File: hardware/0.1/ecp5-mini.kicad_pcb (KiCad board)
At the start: 4 copper layers, 52 x 27 mm, 7 parts, among them J1 Conn_01x40_Male, J2 Conn_01x40_Male

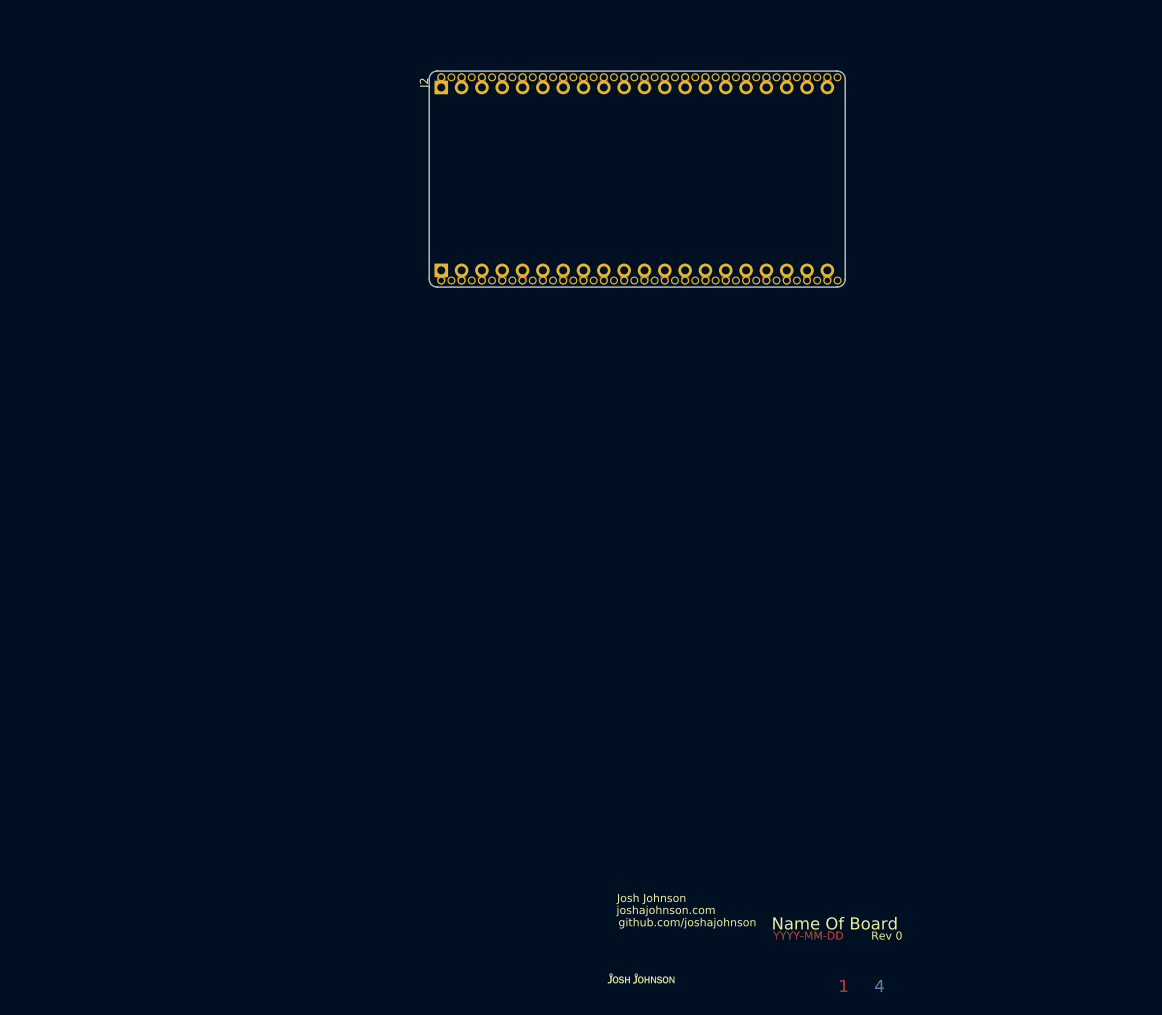
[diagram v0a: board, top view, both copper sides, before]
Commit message: looks like it will fit
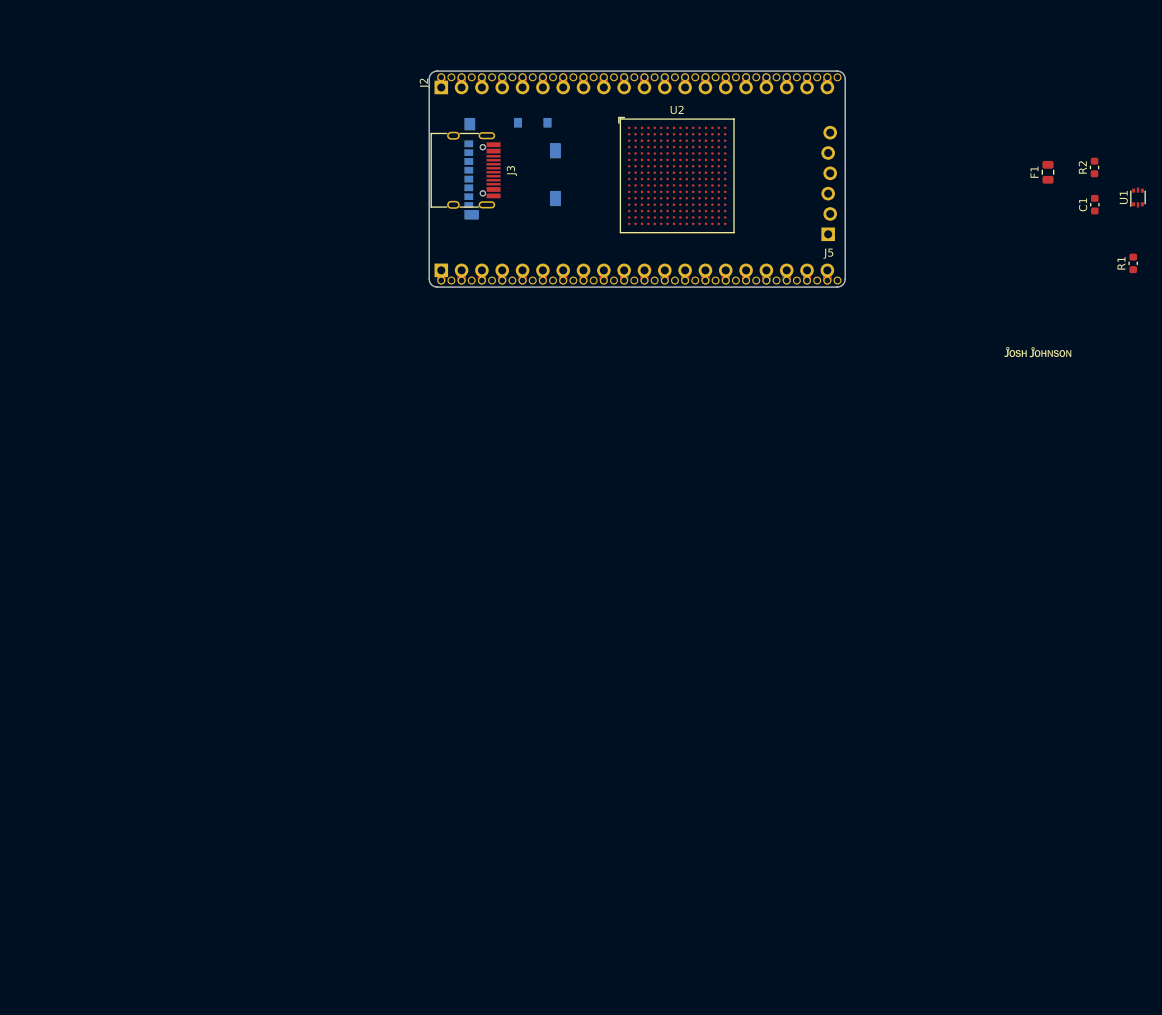
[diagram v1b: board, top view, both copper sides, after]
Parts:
- removed LOGO1: Josh-Details, josh-logos:josh-details
- removed LOGO3: Board-Title, josh-logos:board-title
- removed LOGO5: 4-Layer-Check, josh-logos:4-layer-check
- added C1: 4u7, Capacitor_SMD:C_0603_1608Metric, F.Cu at (199.8, 97.2)
- added F1: 1A, josh-passives-smt:Fuse_0805_2012Metric, F.Cu at (193.9, 93.2)
- added J3: USB_C_Receptacle_USB2.0, josh-connectors:USB_C_U262-161N-4BVC11, F.Cu at (121.5, 92.9)
- added J4: Micro_SD_Card, Connector_Card:microSD_HC_Molex_104031-0811, B.Cu at (127.0, 92.7)
- added J5: JTAG, josh-connectors:STM_6_PIN_THT_Staggered, F.Cu at (166.6, 100.9)
- added R1: 5K1, Resistor_SMD:R_0603_1608Metric, F.Cu at (204.6, 104.5)
- added R2: 5K1, Resistor_SMD:R_0603_1608Metric, F.Cu at (199.8, 92.5)
- added U1: USBLC6-2SC6, Package_TO_SOT_SMD:SOT-666, F.Cu at (205.2, 96.3)
- added U2: ECP5U_12_CABGA256, Package_BGA:BGA-256_14.0x14.0mm_Layout16x16_P0.8mm_Ball0.45mm_Pad0.32mm_NSMD, F.Cu at (147.6, 93.6)
- J1, J2: value Conn_01x40_Male -> S7 Mini
- moved LOGO2 92.7 mm to (206.8, 115.6)
- moved LOGO4 92.7 mm to (192.7, 115.6)

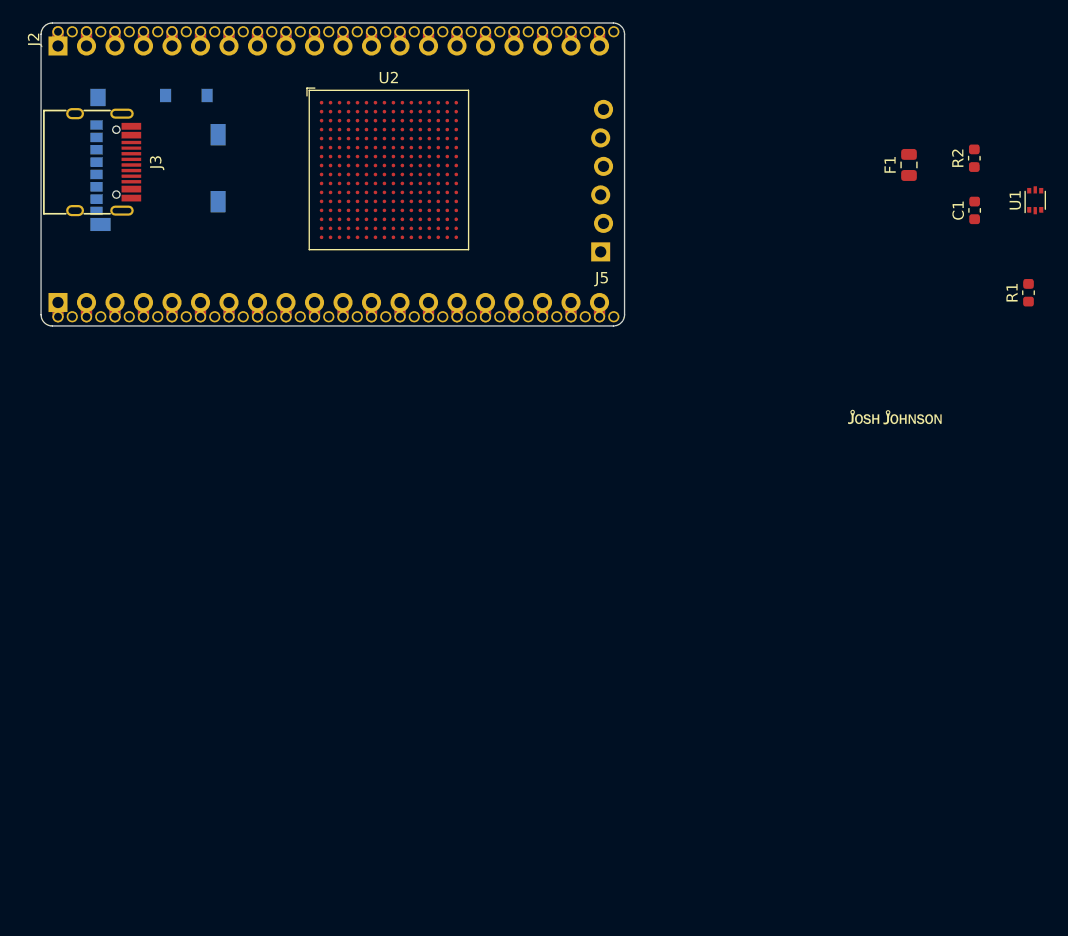
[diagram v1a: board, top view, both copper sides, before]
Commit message: update gitignore
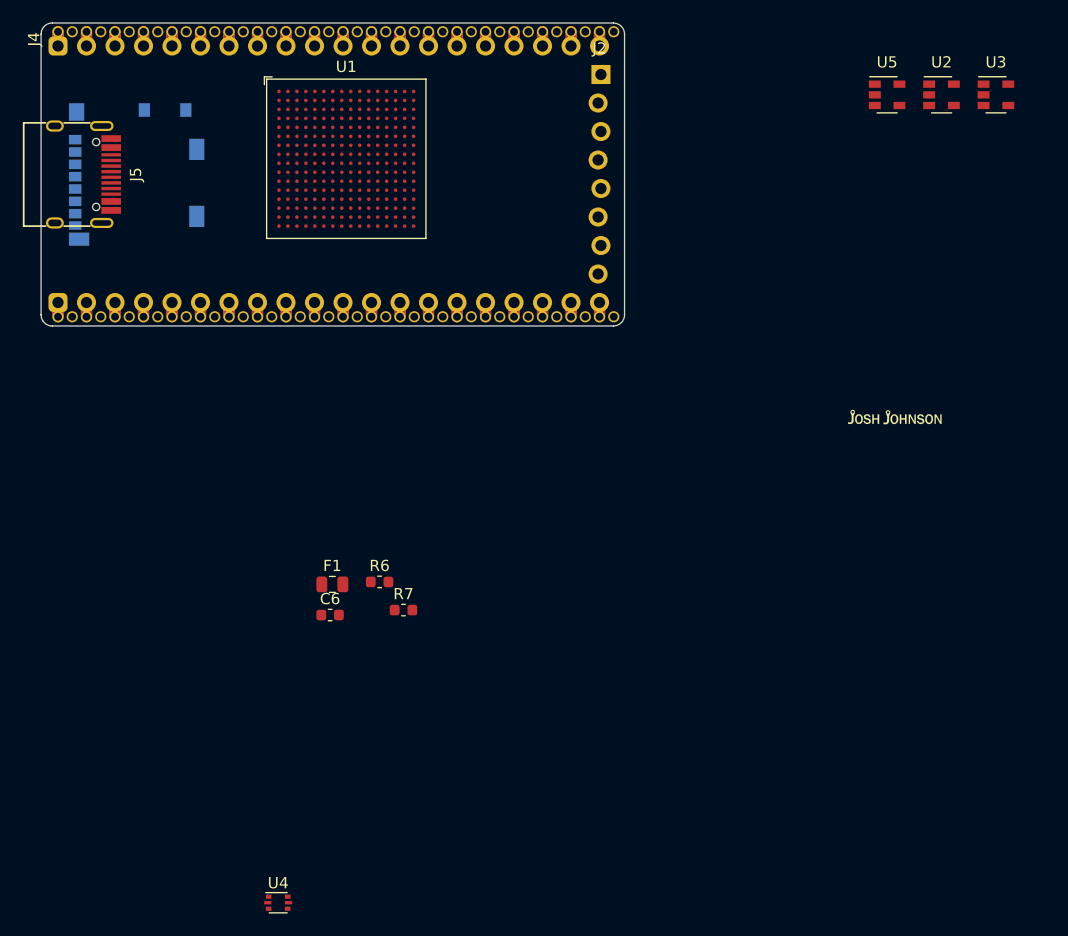
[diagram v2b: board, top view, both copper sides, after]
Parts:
- removed C1: 4u7, Capacitor_SMD:C_0603_1608Metric
- removed R1, R2: 5K1, Resistor_SMD:R_0603_1608Metric
- added C6: 4u7, Capacitor_SMD:C_0603_1608Metric, F.Cu at (142.4, 133.3)
- added R6: 5K1, Resistor_SMD:R_0603_1608Metric, F.Cu at (146.8, 130.3)
- added R7: 5K1, Resistor_SMD:R_0603_1608Metric, F.Cu at (148.9, 132.8)
- added U3: TLV62568DBV, Package_TO_SOT_SMD:SOT-23-5, F.Cu at (201.7, 86.9)
- added U4: USBLC6-2SC6, Package_TO_SOT_SMD:SOT-666, F.Cu at (137.7, 158.9)
- added U5: TLV62568DBV, Package_TO_SOT_SMD:SOT-23-5, F.Cu at (192.0, 86.9)
- J1: value S7 Mini -> Micro_SD_Card; footprint josh-connectors:ECP5-Mini-Edge-20x2.54-40x1.27 -> Connector_Card:microSD_HC_Molex_104031-0811
- J2: value S7 Mini -> JTAG; footprint josh-connectors:ECP5-Mini-Edge-20x2.54-40x1.27 -> josh-connectors:8_PIN_THT_Staggered
- J3: value USB_C_Receptacle_USB2.0 -> S7 Mini; footprint josh-connectors:USB_C_U262-161N-4BVC11 -> josh-connectors:ECP5-Mini-Edge-20x2.54-40x1.27; moved to B.Cu
- J4: value Micro_SD_Card -> S7 Mini; footprint Connector_Card:microSD_HC_Molex_104031-0811 -> josh-connectors:ECP5-Mini-Edge-20x2.54-40x1.27; moved to F.Cu
- J5: value JTAG -> USB_C_Receptacle_USB2.0; footprint josh-connectors:STM_6_PIN_THT_Staggered -> josh-connectors:USB_C_U262-161N-4BVC11
- U1: value USBLC6-2SC6 -> ECP5U_12_CABGA256; footprint Package_TO_SOT_SMD:SOT-666 -> Package_BGA:BGA-256_14.0x14.0mm_Layout16x16_P0.8mm_Ball0.45mm_Pad0.32mm_NSMD
- U2: value ECP5U_12_CABGA256 -> TLV73325PDBV; footprint Package_BGA:BGA-256_14.0x14.0mm_Layout16x16_P0.8mm_Ball0.45mm_Pad0.32mm_NSMD -> Package_TO_SOT_SMD:SOT-23-5
- moved F1 63.5 mm to (142.6, 130.5), turned to 0 degrees
- moved U1 61.5 mm to (143.8, 92.6), turned to 0 degrees
- moved U2 49.7 mm to (196.8, 86.9)
- moved J2 48.3 mm to (166.4, 85.1), turned to 0 degrees
- moved J5 47.4 mm to (119.7, 94.0), turned to -90 degrees
- moved J4 13.5 mm to (118.1, 82.5), turned to 90 degrees
- moved J1 13.4 mm to (125.1, 94.0)
- moved J3 13.0 mm to (118.1, 105.4)
- renumbered LOGO4 to LOGO1
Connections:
- net Net-(J2-Pad5) renamed /FPGA Config/TCK
- net Net-(J2-Pad6) renamed /FPGA Config/TDO
- net Net-(J2-Pad7) renamed /FPGA Config/TDI
- net Net-(J2-Pad8) renamed /FPGA Config/TMS
- F1 pad 1: Net-(C1-Pad1) -> Net-(C6-Pad1)
- F1 pad 2: VBUS -> +5V
- J2 pad 1: Net-(J2-Pad1) -> GND
- J2 pad 2: Net-(J2-Pad2) -> +5V
- J2 pad 3: Net-(J2-Pad3) -> +3V3
- J2 pad 4: Net-(J2-Pad4) -> GND

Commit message: power + leds + hyperram
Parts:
- added C1: 4u7, Capacitor_SMD:C_0603_1608Metric, F.Cu at (154.4, 129.4)
- added C10: 6p8, Capacitor_SMD:C_0603_1608Metric, F.Cu at (162.4, 135.1)
- added C11: 10u, Capacitor_SMD:C_0603_1608Metric, F.Cu at (181.8, 148.6)
- added C12: 100n, Capacitor_SMD:C_0402_1005Metric, F.Cu at (182.0, 152.0)
- added C13: 100n, Capacitor_SMD:C_0402_1005Metric, F.Cu at (180.0, 132.6)
- added C14: 470n, Capacitor_SMD:C_0402_1005Metric, F.Cu at (178.1, 138.4)
- added C15: 100n, Capacitor_SMD:C_0402_1005Metric, F.Cu at (176.1, 133.1)
- added C16: 100n, Capacitor_SMD:C_0402_1005Metric, F.Cu at (182.0, 138.4)
- added C17: 100n, Capacitor_SMD:C_0402_1005Metric, F.Cu at (180.0, 135.5)
- added C18: 100n, Capacitor_SMD:C_0402_1005Metric, F.Cu at (182.0, 141.3)
- added C2: 4u7, Capacitor_SMD:C_0603_1608Metric, F.Cu at (156.9, 129.4)
- added C3: 1u, Capacitor_SMD:C_0603_1608Metric, F.Cu at (164.9, 135.1)
- added C4: 1u, Capacitor_SMD:C_0603_1608Metric, F.Cu at (154.8, 125.4)
- added C5: 10u, Capacitor_SMD:C_0603_1608Metric, F.Cu at (159.8, 130.4)
- added C7: 22u, Capacitor_SMD:C_0603_1608Metric, F.Cu at (164.9, 139.1)
- added C8: 22u, Capacitor_SMD:C_0603_1608Metric, F.Cu at (162.4, 131.1)
- added C9: 6p8, Capacitor_SMD:C_0603_1608Metric, F.Cu at (159.8, 134.5)
- added D1: PINK, LED_SMD:LED_0603_1608Metric, F.Cu at (164.9, 131.1)
- added D2: LED, LED_SMD:LED_0603_1608Metric, F.Cu at (170.7, 121.0)
- added L1: 2u2, Inductor_SMD:L_0805_2012Metric, F.Cu at (159.7, 126.2)
- added L2: 2u2, Inductor_SMD:L_0805_2012Metric, F.Cu at (154.6, 121.2)
- added Q1: BSS138, Package_TO_SOT_SMD:SOT-23, F.Cu at (180.8, 128.9)
- added R1: 210k, Resistor_SMD:R_0402_1005Metric, F.Cu at (157.6, 132.9)
- added R10: 22R, Resistor_SMD:R_0402_1005Metric, F.Cu at (178.1, 132.6)
- added R11: 1K5, Resistor_SMD:R_0402_1005Metric, F.Cu at (182.0, 132.6)
- added R12: 5K1, Resistor_SMD:R_0402_1005Metric, F.Cu at (175.5, 130.2)
- added R13: 1k, Resistor_SMD:R_0402_1005Metric, F.Cu at (182.0, 135.5)
- added R14: 1k, Resistor_SMD:R_0402_1005Metric, F.Cu at (178.1, 135.5)
- added R15: 1k, Resistor_SMD:R_0402_1005Metric, F.Cu at (173.5, 130.3)
- added R16: 1k, Resistor_SMD:R_0402_1005Metric, F.Cu at (180.0, 138.4)
- added R17: 1k, Resistor_SMD:R_0402_1005Metric, F.Cu at (172.5, 127.4)
- added R18: 1k, Resistor_SMD:R_0402_1005Metric, F.Cu at (171.5, 130.3)
- added R19: 5K1, Resistor_SMD:R_0402_1005Metric, F.Cu at (177.5, 128.1)
- added R2: 47k, Resistor_SMD:R_0402_1005Metric, F.Cu at (162.7, 138.6)
- added R20: 51R, Resistor_SMD:R_0402_1005Metric, F.Cu at (171.0, 124.5)
- added R21: 1K5, Resistor_SMD:R_0402_1005Metric, F.Cu at (170.5, 127.4)
- added R3: 84k5, Resistor_SMD:R_0402_1005Metric, F.Cu at (160.1, 137.9)
- added R4: 100k, Resistor_SMD:R_0402_1005Metric, F.Cu at (155.6, 132.9)
- added R5: 5K1, Resistor_SMD:R_0402_1005Metric, F.Cu at (157.2, 125.5)
- added R8: 10K, Resistor_SMD:R_0402_1005Metric, F.Cu at (176.1, 136.1)
- added R9: 22R, Resistor_SMD:R_0402_1005Metric, F.Cu at (174.1, 133.2)
- added RN1: 10k, Resistor_SMD:R_Array_Convex_4x0402, F.Cu at (175.0, 127.3)
- added SW1: SW_Push, josh-buttons-switches:SW_Push_PTS815, F.Cu at (174.2, 122.4)
- added TP1: 2v5, TestPoint:TestPoint_Pad_D1.5mm, F.Cu at (163.7, 126.6)
- added TP2: 3V3, TestPoint:TestPoint_Pad_D1.5mm, F.Cu at (158.6, 121.5)
- added TP3: 1v1, TestPoint:TestPoint_Pad_D1.5mm, F.Cu at (163.7, 121.5)
- added U6: W25Q128JVSIQ, Package_SON:WSON-8-1EP_6x5mm_P1.27mm_EP3.4x4.3mm, F.Cu at (103.7, 96.8)
- added U7: S27KL0641, josh-bga:BGA-24_5x5_6.0x8.0mm, F.Cu at (103.8, 89.5)
- J2: footprint josh-connectors:8_PIN_THT_Staggered -> josh-connectors:STM_6_PIN_THT_Staggered
- R6, R7: footprint Resistor_SMD:R_0603_1608Metric -> Resistor_SMD:R_0402_1005Metric
- moved J2 69.9 mm to (98.4, 101.3), turned to 180 degrees
- moved U1 25.9 mm to (118.0, 94.8), turned to 180 degrees
- moved J5 25.4 mm to (145.1, 95.0), turned to 90 degrees
- moved J3 20.4 mm to (97.7, 106.4)
- moved J4 20.4 mm to (97.7, 83.5)
- moved J1 14.6 mm to (139.7, 95.0), turned to 90 degrees
- moved U5 3.20 mm to (188.9, 86.1), turned to 180 degrees
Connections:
- net Net-(J1-Pad1) renamed /Hyperram / Micro SD/SD.DAT2
- net Net-(J1-Pad10) renamed /Hyperram / Micro SD/SD.DETA
- net Net-(J1-Pad2) renamed /Hyperram / Micro SD/SD.DAT3
- net Net-(J1-Pad3) renamed /Hyperram / Micro SD/SD.CMD
- net Net-(J1-Pad7) renamed /Hyperram / Micro SD/SD.DAT0
- net Net-(J1-Pad8) renamed /Hyperram / Micro SD/SD.DAT1
- net Net-(J1-Pad9) renamed /Hyperram / Micro SD/SD.DETB
- J1 pad 11: Net-(J1-Pad11) -> GND
- J1 pad 4: Net-(J1-Pad4) -> +3V3
- J1 pad 5: Net-(J1-Pad5) -> +3V3
- J1 pad 6: Net-(J1-Pad6) -> GND
- J2 pad 1: GND -> +3V3
- J2 pad 2: +5V -> GND
- J2 pad 3: +3V3 -> /FPGA Config/TCK
- J2 pad 4: GND -> /FPGA Config/TDO
- J2 pad 5: /FPGA Config/TCK -> /FPGA Config/TDI
- J2 pad 6: /FPGA Config/TDO -> /FPGA Config/TMS
- U1 pad L6: Net-(U1-PadL6) -> +3V3
- U1 pad M10: Net-(U1-PadM10) -> /FPGA Config/TDO
- U1 pad M7: Net-(U1-PadM7) -> /FPGA Config/CFG.IO2
- U1 pad N10: Net-(U1-PadN10) -> /FPGA Config/CFG_0
- U1 pad N7: Net-(U1-PadN7) -> /FPGA Config/CFG.IO3
- U1 pad N8: Net-(U1-PadN8) -> /FPGA Config/CFG.CS
- U1 pad N9: Net-(U1-PadN9) -> /FPGA Config/CFG.CLK
- U1 pad P10: Net-(U1-PadP10) -> /FPGA Config/CFG_1
- U1 pad P9: Net-(U1-PadP9) -> /FPGA Config/CFG.CDONE
- U1 pad R10: Net-(U1-PadR10) -> /FPGA Config/CFG_2
- U1 pad R11: Net-(U1-PadR11) -> /FPGA Config/TDI
- U1 pad R8: Net-(U1-PadR8) -> /FPGA Config/nBTN_USR
- U1 pad R9: Net-(U1-PadR9) -> /FPGA Config/nFPGA_RST
- U1 pad T10: Net-(U1-PadT10) -> /FPGA Config/TCK
- U1 pad T11: Net-(U1-PadT11) -> /FPGA Config/TMS
- U1 pad T7: Net-(U1-PadT7) -> /FPGA Config/CFG.IO1
- U1 pad T8: Net-(U1-PadT8) -> /FPGA Config/CFG.IO0
- U4 pad 4: /FPGA Config/USB_D+ -> Net-(R10-Pad2)
- U4 pad 6: /FPGA Config/USB_D- -> Net-(R9-Pad1)
